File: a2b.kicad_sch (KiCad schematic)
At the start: 10 parts, among them J1 RAPC722X, J2 PPPC031LFBN-RC, J3 NMJ6HCD2, J4 PPPC031LFBN-RC, J5 NMJ6HCD2, J6 PPPC031LFBN-RC, SW1 ANT21SECQE, SW2 ANT21SECQE

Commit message: UPDATE PCB
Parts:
- removed J2, J4, J6: PPPC031LFBN-RC, PPPC031LFBN:CONN_PPPC031LFBN-RC_SUL, symbol PPPC031LFBN_RC:PPPC031LFBN-RC
- removed SW1, SW2: ANT21SECQE, ANT21SECQE:SW6_ANT21SECQE_CRS, symbol 2026-04-30_17-37-32:ANT21SECQE
- added J10, J11, J12, J13, J14, J15, J16, J17, J18, J19, J20, J21, J8, J9: Conn_01x01, TestPoint:TestPoint_THTPad_D2.0mm_Drill1.0mm, symbol Connector_Generic:Conn_01x01
- added J2, J4: Conn_01x01, TestPoint:TestPoint_Pad_D1.5mm, symbol Connector_Generic:Conn_01x01
- added J6: NEG1, TestPoint:TestPoint_THTPad_D2.0mm_Drill1.0mm, symbol Connector_Generic:Conn_01x01
- added J7: POS1, TestPoint:TestPoint_THTPad_D2.0mm_Drill1.0mm, symbol Connector_Generic:Conn_01x01
- added SW1, SW2: ANT21SECQE, ANT21SECQE:SW6_ANT21SECQE_CRS, symbol ANT21SECQE:ANT21SECQE
- added U1: ANT13SECQE, footprints:ANT13SEC_CRS, symbol ANT13SECQE:ANT13SECQE
- R1: footprint Resistor_THT:R_Bare_Metal_Element_L12.4mm_W4.8mm_P11.40mm -> Resistor_THT:R_Axial_DIN0207_L6.3mm_D2.5mm_P10.16mm_Horizontal
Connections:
- net at R1.1: now also U1.2; no longer J1.PIN
- net at J5.T: now also SW2.5
- net at J1.SLEEVE, J3.RN, J3.SN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: now also J2.1 (Pin_1), J6.1 (Pin_1), J8.1 (Pin_1), SW1.3, SW1.6, SW2.1, SW2.4; no longer D1.1 (K)
- net at J5.R: now also SW2.2
- net at J5.S: now also J10.1 (Pin_1), J19.1 (Pin_1)
- net at J3.R: now also SW1.5
- net at J3.S: now also J15.1 (Pin_1), J18.1 (Pin_1)
- net at J3.T: now also SW1.2
- new net: J11.1 (Pin_1), J20.1 (Pin_1), SW2.3
- new net: D1.1 (K), J4.1 (Pin_1), J7.1 (Pin_1), J9.1 (Pin_1)
- new net: J1.PIN, U1.1
- new net: J12.1 (Pin_1), J21.1 (Pin_1), SW2.6
- new net: J14.1 (Pin_1), J17.1 (Pin_1), SW1.4
- new net: J13.1 (Pin_1), J16.1 (Pin_1), SW1.1
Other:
- moved on the sheet: J3

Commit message: update pcb
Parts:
- B1+1: renamed from J4; footprint TestPoint:TestPoint_Pad_D1.5mm -> TestPoint:TestPoint_THTPad_D1.5mm_Drill0.7mm
- B1-1: renamed from J2; footprint TestPoint:TestPoint_Pad_D1.5mm -> TestPoint:TestPoint_THTPad_D1.5mm_Drill0.7mm
- B2+1: renamed from J9; footprint TestPoint:TestPoint_THTPad_D2.0mm_Drill1.0mm -> TestPoint:TestPoint_THTPad_D1.5mm_Drill0.7mm
- B2-1: renamed from J8; footprint TestPoint:TestPoint_THTPad_D2.0mm_Drill1.0mm -> TestPoint:TestPoint_THTPad_D1.5mm_Drill0.7mm
- B_R_IN1: renamed from J17; footprint TestPoint:TestPoint_THTPad_D2.0mm_Drill1.0mm -> TestPoint:TestPoint_THTPad_D1.5mm_Drill0.7mm
- B_R_OUT1: renamed from J20; footprint TestPoint:TestPoint_THTPad_D2.0mm_Drill1.0mm -> TestPoint:TestPoint_THTPad_D1.5mm_Drill0.7mm
- B_S_IN1: renamed from J18; footprint TestPoint:TestPoint_THTPad_D2.0mm_Drill1.0mm -> TestPoint:TestPoint_THTPad_D1.5mm_Drill0.7mm
- B_S_OUT1: renamed from J21; footprint TestPoint:TestPoint_THTPad_D2.0mm_Drill1.0mm -> TestPoint:TestPoint_THTPad_D1.5mm_Drill0.7mm
- B_T_IN1: renamed from J16; footprint TestPoint:TestPoint_THTPad_D2.0mm_Drill1.0mm -> TestPoint:TestPoint_THTPad_D1.5mm_Drill0.7mm
- B_T_OUT1: renamed from J19; footprint TestPoint:TestPoint_THTPad_D2.0mm_Drill1.0mm -> TestPoint:TestPoint_THTPad_D1.5mm_Drill0.7mm
- F1+1: renamed from J7; value POS1 -> Conn_01x01; footprint TestPoint:TestPoint_THTPad_D2.0mm_Drill1.0mm -> TestPoint:TestPoint_THTPad_D1.5mm_Drill0.7mm
- F1-1: renamed from J6; value NEG1 -> Conn_01x01; footprint TestPoint:TestPoint_THTPad_D2.0mm_Drill1.0mm -> TestPoint:TestPoint_THTPad_D1.5mm_Drill0.7mm
- R_IN1: renamed from J14; footprint TestPoint:TestPoint_THTPad_D2.0mm_Drill1.0mm -> TestPoint:TestPoint_THTPad_D1.5mm_Drill0.7mm
- R_OUT1: renamed from J11; footprint TestPoint:TestPoint_THTPad_D2.0mm_Drill1.0mm -> TestPoint:TestPoint_THTPad_D1.5mm_Drill0.7mm
- S_IN1: renamed from J15; footprint TestPoint:TestPoint_THTPad_D2.0mm_Drill1.0mm -> TestPoint:TestPoint_THTPad_D1.5mm_Drill0.7mm
- S_OUT1: renamed from J12; footprint TestPoint:TestPoint_THTPad_D2.0mm_Drill1.0mm -> TestPoint:TestPoint_THTPad_D1.5mm_Drill0.7mm
- T_IN1: renamed from J13; footprint TestPoint:TestPoint_THTPad_D2.0mm_Drill1.0mm -> TestPoint:TestPoint_THTPad_D1.5mm_Drill0.7mm
- T_OUT1: renamed from J10; footprint TestPoint:TestPoint_THTPad_D2.0mm_Drill1.0mm -> TestPoint:TestPoint_THTPad_D1.5mm_Drill0.7mm
- renumbered J3 to AUDIO_IN1, SW1 to AUDIO_IN_SW1, J5 to AUDIO_OUT1, SW2 to AUDIO_OUT_SW1, J1 to DC_IN1, U1 to POWERSWITCH1
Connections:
- net at B_R_OUT1.1 (Pin_1), R_OUT1.1 (Pin_1): now also AUDIO_OUT_SW1.4; no longer AUDIO_OUT_SW1.3
- net at AUDIO_OUT1.R: now also AUDIO_OUT_SW1.5; no longer AUDIO_OUT_SW1.2
- net at B_T_OUT1.1 (Pin_1), T_OUT1.1 (Pin_1): now also AUDIO_OUT_SW1.1; no longer AUDIO_OUT1.S
- net at AUDIO_OUT1.T: now also AUDIO_OUT_SW1.2; no longer AUDIO_OUT_SW1.5
- net at AUDIO_OUT_SW1.6, B_S_OUT1.1 (Pin_1), S_OUT1.1 (Pin_1): now also AUDIO_OUT1.RN, AUDIO_OUT1.S, AUDIO_OUT1.SN, AUDIO_OUT1.TN, AUDIO_OUT_SW1.3
- new net: B1-1.1 (Pin_1), B2-1.1 (Pin_1), DC_IN1.SLEEVE, F1-1.1 (Pin_1)
- new net: AUDIO_IN1.RN, AUDIO_IN1.SN, AUDIO_IN1.TN, AUDIO_IN_SW1.3, AUDIO_IN_SW1.6
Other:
- moved on the sheet: AUDIO_IN_SW1, AUDIO_OUT1, AUDIO_OUT_SW1, POWERSWITCH1, R_OUT1, S_OUT1, T_OUT1

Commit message: update pcb and schematic
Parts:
- removed B1+1, B1-1, B2+1, B2-1, F1+1, F1-1: Conn_01x01, TestPoint:TestPoint_THTPad_D1.5mm_Drill0.7mm, symbol Connector_Generic:Conn_01x01
- added U1, U2, U3: (no value), Connector_PinHeader_2.54mm:PinHeader_1x02_P2.54mm_Vertical, symbol customHeaders:2pinHeader
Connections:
- net at D1.1 (K): now also U1.1, U2.1, U3.1
- net at DC_IN1.SLEEVE: now also U1.2, U2.2, U3.2

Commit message: update pcb
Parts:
- removed B_R_IN1, B_R_OUT1, B_S_IN1, B_S_OUT1, B_T_IN1, B_T_OUT1, R_IN1, R_OUT1, S_IN1, S_OUT1, T_IN1, T_OUT1: Conn_01x01, TestPoint:TestPoint_THTPad_D1.5mm_Drill0.7mm, symbol Connector_Generic:Conn_01x01
- added pinout1, pinout2, pinout3, pinout4: (no value), Connector_PinHeader_2.54mm:PinHeader_1x03_P2.54mm_Vertical, symbol customHeaders:3pinHeader
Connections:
- net at AUDIO_OUT_SW1.4: now also pinout3.2, pinout4.2
- net at AUDIO_IN1.S: now also pinout1.1, pinout2.1
- net at AUDIO_OUT1.RN, AUDIO_OUT1.S, AUDIO_OUT1.SN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: now also pinout3.1, pinout4.1
- net at AUDIO_IN_SW1.4: now also pinout1.2, pinout2.2
- net at AUDIO_IN_SW1.1: now also pinout1.3, pinout2.3
- net at AUDIO_OUT_SW1.1: now also pinout3.3, pinout4.3

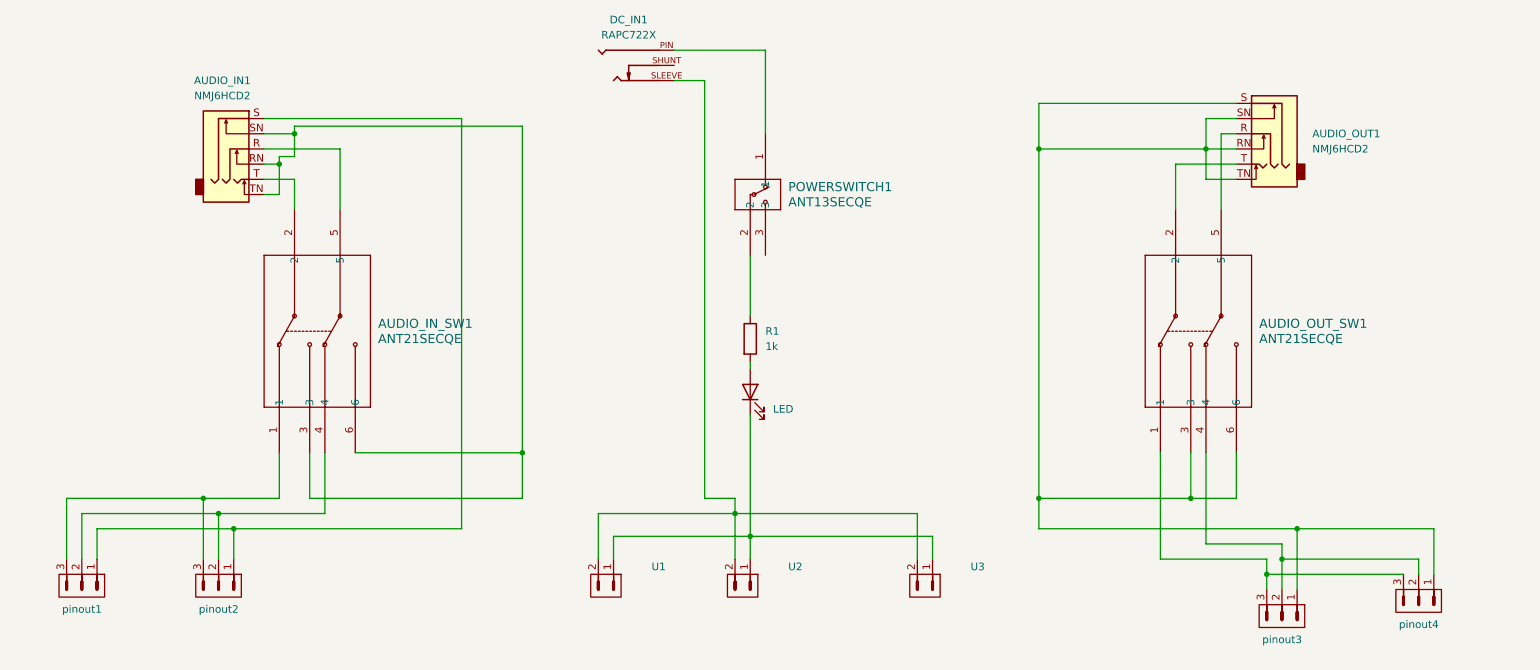
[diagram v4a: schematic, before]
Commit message: update pcb silkscreens
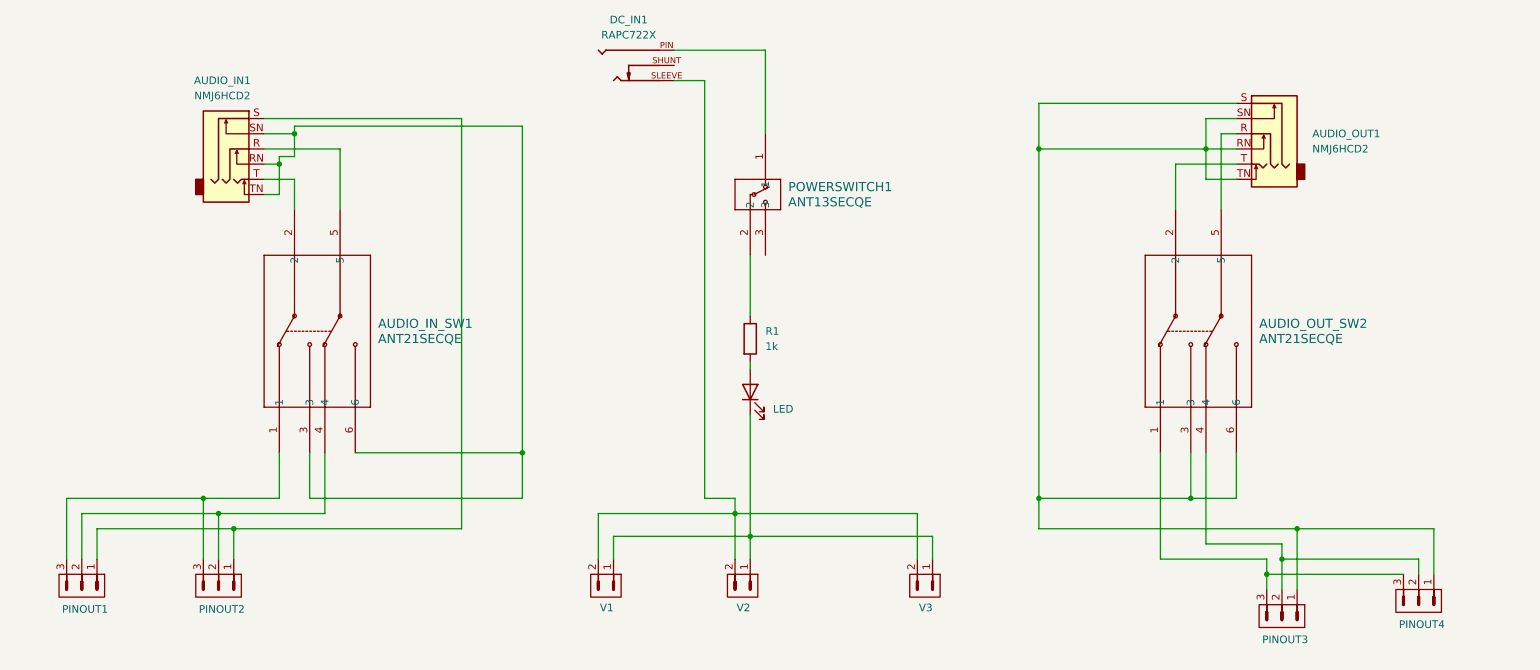
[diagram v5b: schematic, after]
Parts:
- renumbered AUDIO_OUT_SW1 to AUDIO_OUT_SW2, pinout1 to PINOUT1, pinout2 to PINOUT2, pinout3 to PINOUT3, pinout4 to PINOUT4, U1 to V1, U2 to V2, U3 to V3
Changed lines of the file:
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@@
 		(in_pos_files yes)
 		(dnp no)
-		(fields_autoplaced yes)
-		(property "Reference" "U1"
-			(at 130.81 128.2699 90)
+		(property "Reference" "V1"
+			(at 122.174 135.128 90)
 			(show_name no)
 			(do_not_autoplace no)
@@
 			(project "a2b"
 				(path "/2fb67ef4-3b78-48fd-981f-3213cdbc031d"
-					(reference "U1")
+					(reference "V1")
 					(unit 1)
 				)
@@
 		(in_pos_files yes)
 		(dnp no)
-		(fields_autoplaced yes)
-		(property "Reference" "U3"
-			(at 184.15 128.2699 90)
+		(property "Reference" "V3"
+			(at 175.514 135.128 90)
 			(show_name no)
 			(do_not_autoplace no)
@@
 			(project "a2b"
 				(path "/2fb67ef4-3b78-48fd-981f-3213cdbc031d"
-					(reference "U3")
+					(reference "V3")
 					(unit 1)
 				)
@@
 		(in_pos_files yes)
 		(dnp no)
-		(fields_autoplaced yes)
-		(property "Reference" "U2"
-			(at 153.67 128.2699 90)
+		(property "Reference" "V2"
+			(at 145.034 135.128 90)
 			(show_name no)
 			(do_not_autoplace no)
@@
 			(project "a2b"
 				(path "/2fb67ef4-3b78-48fd-981f-3213cdbc031d"
-					(reference "U2")
+					(reference "V2")
 					(unit 1)
 				)
@@
 		(dnp no)
 		(fields_autoplaced yes)
-		(property "Reference" "AUDIO_OUT_SW1"
+		(property "Reference" "AUDIO_OUT_SW2"
 			(at 232.41 87.6299 90)
 			(show_name no)
@@
 			(project "a2b"
 				(path "/2fb67ef4-3b78-48fd-981f-3213cdbc031d"
-					(reference "AUDIO_OUT_SW1")
+					(reference "AUDIO_OUT_SW2")
 					(unit 1)
 				)
@@
 		(in_pos_files yes)
 		(dnp no)
-		(property "Reference" "pinout3"
+		(property "Reference" "PINOUT3"
 			(at 232.918 140.462 90)
 			(show_name no)
@@
 			(project "a2b"
 				(path "/2fb67ef4-3b78-48fd-981f-3213cdbc031d"
-					(reference "pinout3")
+					(reference "PINOUT3")
 					(unit 1)
 				)
@@
 		(in_pos_files yes)
 		(dnp no)
-		(property "Reference" "pinout2"
+		(property "Reference" "PINOUT2"
 			(at 55.118 135.382 90)
 			(show_name no)
@@
 			(project "a2b"
 				(path "/2fb67ef4-3b78-48fd-981f-3213cdbc031d"
-					(reference "pinout2")
+					(reference "PINOUT2")
 					(unit 1)
 				)
@@
 		(in_pos_files yes)
 		(dnp no)
-		(property "Reference" "pinout4"
+		(property "Reference" "PINOUT4"
 			(at 255.778 137.922 90)
 			(show_name no)
@@
 			(project "a2b"
 				(path "/2fb67ef4-3b78-48fd-981f-3213cdbc031d"
-					(reference "pinout4")
+					(reference "PINOUT4")
 					(unit 1)
 				)
@@
 		(in_pos_files yes)
 		(dnp no)
-		(property "Reference" "pinout1"
+		(property "Reference" "PINOUT1"
 			(at 32.258 135.382 90)
 			(show_name no)
@@
 			(project "a2b"
 				(path "/2fb67ef4-3b78-48fd-981f-3213cdbc031d"
-					(reference "pinout1")
-					(unit 1)
-				)
+					(reference "PINOUT1")
+					(unit 1)
+				)

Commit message: swap to dip switches Signed-off-by: MrMentalFlower <samuelejpike@gmail.com>
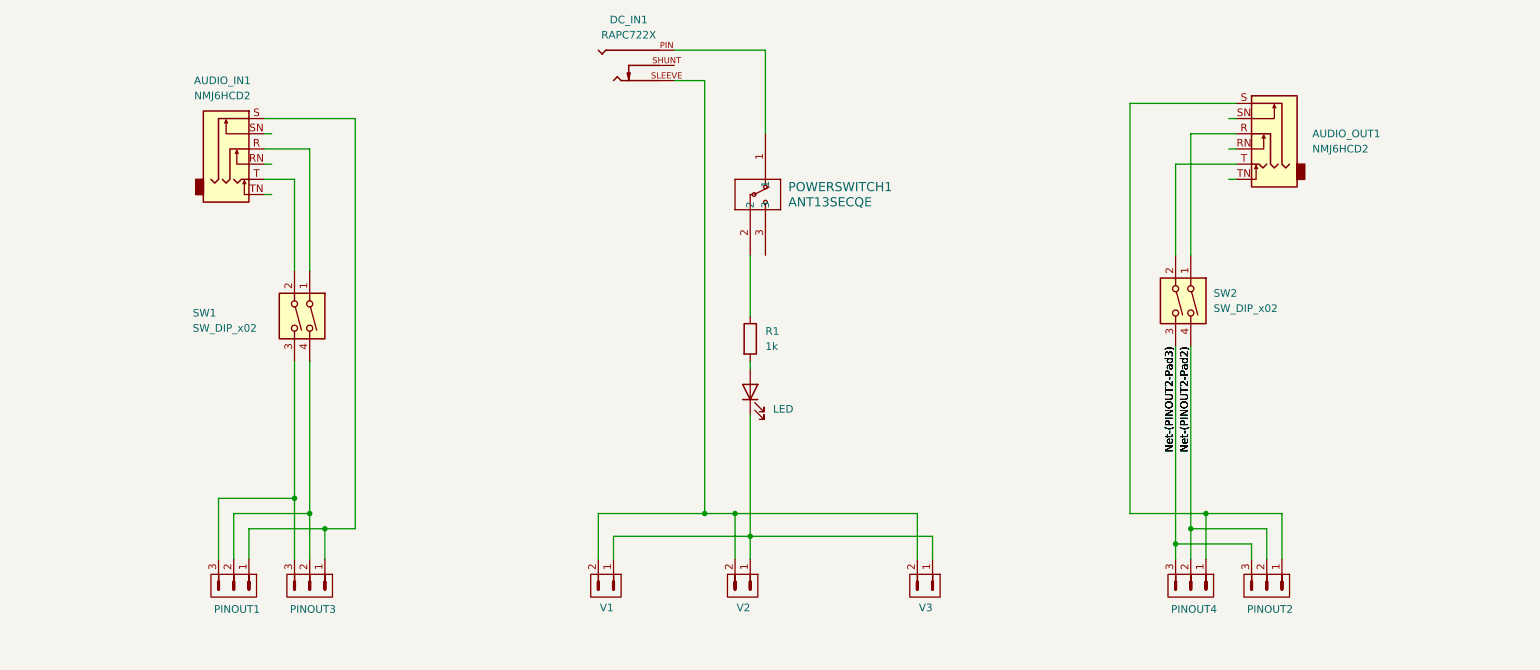
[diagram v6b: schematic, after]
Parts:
- removed AUDIO_IN_SW1, AUDIO_OUT_SW2: ANT21SECQE, ANT21SECQE:SW6_ANT21SECQE_CRS, symbol ANT21SECQE:ANT21SECQE
- added SW1, SW2: SW_DIP_x02, Button_Switch_THT:SW_DIP_SPSTx02_Slide_9.78x7.26mm_W7.62mm_P2.54mm, symbol Switch:SW_DIP_x02
- D1: KiLib_Generator (none) -> LED/THT
- PINOUT1, V1, V2, V3: KiLib_Generator (none) -> connector/pin_header_socket
- PINOUT2: renamed from PINOUT4; KiLib_Generator (none) -> connector/pin_header_socket
- PINOUT3: renamed from PINOUT2; KiLib_Generator (none) -> connector/pin_header_socket
- PINOUT4: renamed from PINOUT3; KiLib_Generator (none) -> connector/pin_header_socket
- R1: KiLib_Generator (none) -> resistor/THT
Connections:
- net at AUDIO_OUT1.R: now also SW2.1
- net at AUDIO_OUT1.S, PINOUT2.1, PINOUT4.1: no longer AUDIO_OUT1.RN, AUDIO_OUT1.SN, AUDIO_OUT1.TN
- net at AUDIO_OUT1.T: now also SW2.2
- net at PINOUT1.3, PINOUT3.3: now also SW1.3
- net at AUDIO_IN1.T: now also SW1.2
- net at PINOUT1.2, PINOUT3.2: now also SW1.4
- net at AUDIO_IN1.R: now also SW1.1
- net Net-(PINOUT2-Pad3): now reaches PINOUT2.3, PINOUT4.3
- net Net-(PINOUT2-Pad3): now also SW2.3
- net Net-(PINOUT2-Pad2): now reaches PINOUT2.2, PINOUT4.2
- net Net-(PINOUT2-Pad2): now also SW2.4
- now unconnected: AUDIO_IN1.RN, AUDIO_IN1.SN, AUDIO_IN1.TN
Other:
- moved on the sheet: PINOUT1, PINOUT2, PINOUT3, PINOUT4

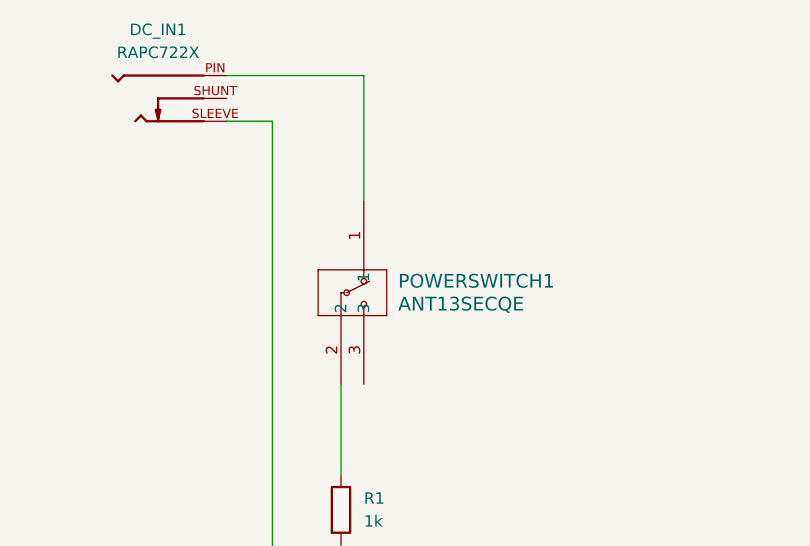
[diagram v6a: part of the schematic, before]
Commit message: update dips switches and silk screen
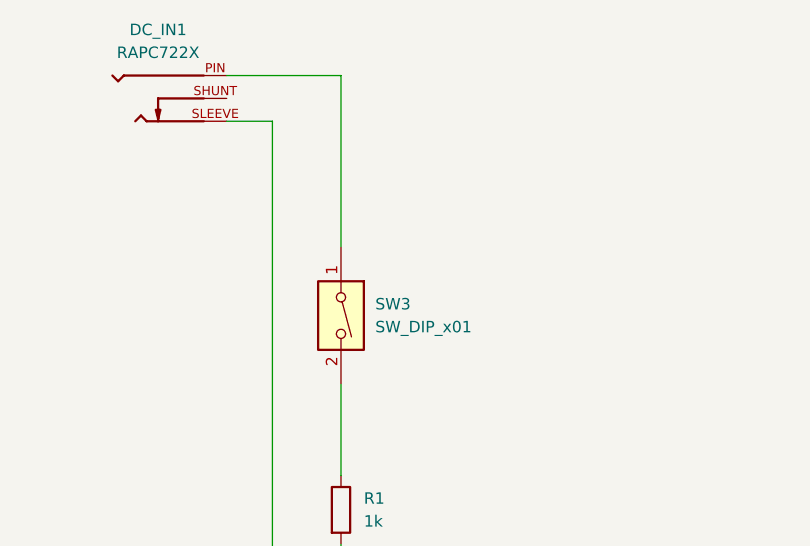
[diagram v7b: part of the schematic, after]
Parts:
- removed POWERSWITCH1: ANT13SECQE, footprints:ANT13SEC_CRS, symbol ANT13SECQE:ANT13SECQE
- added SW3: SW_DIP_x01, Button_Switch_THT:SW_DIP_SPSTx01_Slide_9.78x4.72mm_W7.62mm_P2.54mm, symbol Switch:SW_DIP_x01
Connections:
- net at R1.1: now also SW3.2
- net at DC_IN1.PIN: now also SW3.1
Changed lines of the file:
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@@
 	(wire
 		(pts
-			(xy 149.86 41.91) (xy 149.86 55.88)
+			(xy 147.32 41.91) (xy 147.32 60.96)
 		)
 		(stroke
@@
 	(wire
 		(pts
-			(xy 134.62 41.91) (xy 149.86 41.91)
+			(xy 134.62 41.91) (xy 147.32 41.91)
 		)
 		(stroke
@@
 				(path "/2fb67ef4-3b78-48fd-981f-3213cdbc031d"
 					(reference "R1")
+					(unit 1)
+				)
+			)
+		)
+	)
+	(symbol
+		(lib_id "Switch:SW_DIP_x01")
+		(at 147.32 68.58 270)
+		(unit 1)
+		(body_style 1)
+		(exclude_from_sim no)
+		(in_bom yes)
+		(on_board yes)
+		(in_pos_files yes)
+		(dnp no)
+		(fields_autoplaced yes)
+		(property "Reference" "SW3"
+			(at 151.13 67.3099 90)
+			(show_name no)
+			(do_not_autoplace no)
+			(effects
+				(font
+					(size 1.27 1.27)
+				)
+				(justify left)
+			)
+		)
+		(property "Value" "SW_DIP_x01"
+			(at 151.13 69.8499 90)
+			(show_name no)
+			(do_not_autoplace no)
+			(effects
+				(font
+					(size 1.27 1.27)
+				)
+				(justify left)
+			)
+		)
+		(property "Footprint" "Button_Switch_THT:SW_DIP_SPSTx01_Slide_9.78x4.72mm_W7.62mm_P2.54mm"
+			(at 147.32 68.58 0)
+			(hide yes)
+			(show_name no)
+			(do_not_autoplace no)
+			(effects
+				(font
+					(size 1.27 1.27)
+				)
+			)
+		)
+		(property "Datasheet" ""
+			(at 147.32 68.58 0)
+			(hide yes)
+			(show_name no)
+			(do_not_autoplace no)
+			(effects
+				(font
+					(size 1.27 1.27)
+				)
+			)
+		)
+		(property "Description" "1x DIP Switch, Single Pole Single Throw (SPST) switch, small symbol"
+			(at 147.32 68.58 0)
+			(hide yes)
+			(show_name no)
+			(do_not_autoplace no)
+			(effects
+				(font
+					(size 1.27 1.27)
+				)
+			)
+		)
+		(pin "2"
+		)
+		(pin "1"
+		)
+		(instances
+			(project "a2b"
+				(path "/2fb67ef4-3b78-48fd-981f-3213cdbc031d"
+					(reference "SW3")
 					(unit 1)
 				)
@@
 					(unit 1)
 				)
-			)
-		)
-	)
-	(symbol
-		(lib_id "ANT13SECQE:ANT13SECQE")
-		(at 149.86 55.88 270)
-		(unit 1)
-		(body_style 1)
-		(exclude_from_sim no)
-		(in_bom yes)
-		(on_board yes)
-		(in_pos_files yes)
-		(dnp no)
-		(fields_autoplaced yes)
-		(property "Reference" "POWERSWITCH1"
-			(at 153.67 64.7699 90)
-			(show_name no)
-			(do_not_autoplace no)
-			(effects
-				(font
-					(size 1.524 1.524)
-				)
-				(justify left)
-			)
-		)
-		(property "Value" "ANT13SECQE"
-			(at 153.67 67.3099 90)
-			(show_name no)
-			(do_not_autoplace no)
-			(effects
-				(font
-					(size 1.524 1.524)
-				)
-				(justify left)
-			)
-		)
-		(property "Footprint" "footprints:ANT13SEC_CRS"
-			(at 149.86 55.88 0)
-			(hide yes)
-			(show_name no)
-			(do_not_autoplace no)
-			(effects
-				(font
-					(size 1.27 1.27)
-					(italic yes)
-				)
-			)
-		)
-		(property "Datasheet" "ANT13SECQE"
-			(at 149.86 55.88 0)
-			(hide yes)
-			(show_name no)
-			(do_not_autoplace no)
-			(effects
-				(font
-					(size 1.27 1.27)
-					(italic yes)
-				)
-			)
-		)
-		(property "Description" ""
-			(at 149.86 55.88 0)
-			(hide yes)
-			(show_name no)
-			(do_not_autoplace no)
-			(effects
-				(font
-					(size 1.27 1.27)
-				)
-			)
-		)
-		(pin "2"
-		)
-		(pin "3"
-		)
-		(pin "1"
-		)
-		(instances
-			(project "a2b"
-				(path "/2fb67ef4-3b78-48fd-981f-3213cdbc031d"
-					(reference "POWERSWITCH1")
-					(unit 1)
-				)
